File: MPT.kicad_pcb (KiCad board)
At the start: 2 copper layers, 60 x 50 mm, 94 parts, among them J1 USB4105GFA120, J2 ER-TFT2.79-1, Q2 BSS138, SW1 OS102011MA1QN1, SW2 KMR421GULCLFS, SW3 KMR421GULCLFS, SW4 SW_1825910-6, SW5 SW_1825910-6, SW6 SW_1825910-6, SW7 SW_1825910-6, U2 BQ25185, U3 BQ27441-G1, U4 ESP32-S3-WROOM-1-N4R2, U5 RCLAMP0854P.TCT, U6 TPS63030, U7 MIC2841A

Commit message: PCB Layout Connecting
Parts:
- moved D2 19.9 mm to (168.4, 91.7), turned to 90 degrees
- moved R20 19.5 mm to (170.0, 91.7), turned to 90 degrees
- moved R42 9.96 mm to (164.7, 114.5), turned to 90 degrees
- moved R38 8.91 mm to (175.8, 111.5), turned to 0 degrees
- moved C18 7.23 mm to (175.8, 113.1), turned to 180 degrees
- moved R39 7.10 mm to (171.8, 112.5), turned to 0 degrees
- moved C22 6.97 mm to (166.4, 114.5), turned to -90 degrees
- moved R40 6.73 mm to (179.8, 113.1), turned to 0 degrees
- moved C19 6.08 mm to (171.8, 114.1), turned to 180 degrees
- moved C21 6.06 mm to (183.4, 115.9), turned to 0 degrees
- moved C20 4.62 mm to (179.8, 114.7), turned to 180 degrees
- moved R41 4.14 mm to (183.4, 117.5), turned to 180 degrees
- moved R19 1.70 mm to (144.3, 107.8), turned to 0 degrees
- moved R43 1.31 mm to (139.8, 108.5)
- moved C12 1.00 mm to (174.4, 102.6)
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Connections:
- U4 pad 17: /MCU/GPIO_JOYSTICK_UP -> /MCU/RTC_INT
- U4 pad 18: /MCU/GPIO_JOYSTICK_RIGHT -> /MCU/GPIO_BUTTON1
- U4 pad 19: /MCU/GPIO_JOYSTICK_CENTER -> /MCU/GPIO_BUTTON2
- U4 pad 20: /MCU/GPIO_JOYSTICK_LEFT -> /MCU/GPIO_BUTTON3
- U4 pad 21: /MCU/GPIO_JOYSTICK_DOWN -> /MCU/GPIO_BUTTON4
- U4 pad 22: /MCU/RTC_INT -> /MCU/GPIO_JOYSTICK_DOWN
- U4 pad 23: Net-(D2-K) -> /MCU/GPIO_JOYSTICK_RIGHT
- U4 pad 24: unconnected-(U4-IO47-Pad24) -> /MCU/GPIO_JOYSTICK_UP
- U4 pad 25: unconnected-(U4-IO48-Pad25) -> /MCU/GPIO_JOYSTICK_CENTER
- U4 pad 31: /MCU/GPIO_BUTTON2 -> /MCU/GPIO_JOYSTICK_LEFT
- U4 pad 32: /MCU/GPIO_BUTTON3 -> unconnected-(U4-IO39-Pad32)
- U4 pad 33: /MCU/GPIO_BUTTON4 -> unconnected-(U4-IO40-Pad33)
- U4 pad 38: /MCU/GPIO_BUTTON1 -> Net-(D2-K)
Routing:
- net +3V4: track 1.44 -> 149.6 mm, vias 0 -> 14
- net /BMS/STAT2: track 2.67 -> 63.8 mm, vias 0 -> 4
- net /BMS/STAT1: track 3.03 -> 60.1 mm, vias 0 -> 2
- net VBAT: track 17.4 -> 66.5 mm, vias 2 -> 6
- net /MCU/GPIO_JOYSTICK_LEFT: track 0.00 -> 31.1 mm, vias 0 -> 3
- net /MCU/GPIO_BUTTON1: track 0.00 -> 29.2 mm, vias 0 -> 2
- net /MCU/GPIO_BUTTON2: track 0.00 -> 28.4 mm, vias 0 -> 2
- net /MCU/SLEEP_CTRL_PIN: track 0.00 -> 28.1 mm, vias 0 -> 4
- net /MCU/GPIO_JOYSTICK_DOWN: track 0.00 -> 25.3 mm, vias 0 -> 1
- net /MCU/GPIO_JOYSTICK_CENTER: track 0.00 -> 25.0 mm, vias 0 -> 3
- net /MCU/GPIO_JOYSTICK_RIGHT: track 0.00 -> 24.8 mm, vias 0 -> 3
- net /MCU/GPIO_JOYSTICK_UP: track 0.00 -> 22.2 mm, vias 0 -> 3
- net /MCU/GPIO_BUTTON4: track 0.00 -> 19.0 mm
- net /MCU/GPIO_BUTTON3: track 0.00 -> 18.8 mm, vias 0 -> 2
- net /MCU/RTC_INT: track 0.00 -> 17.2 mm, vias 0 -> 2
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
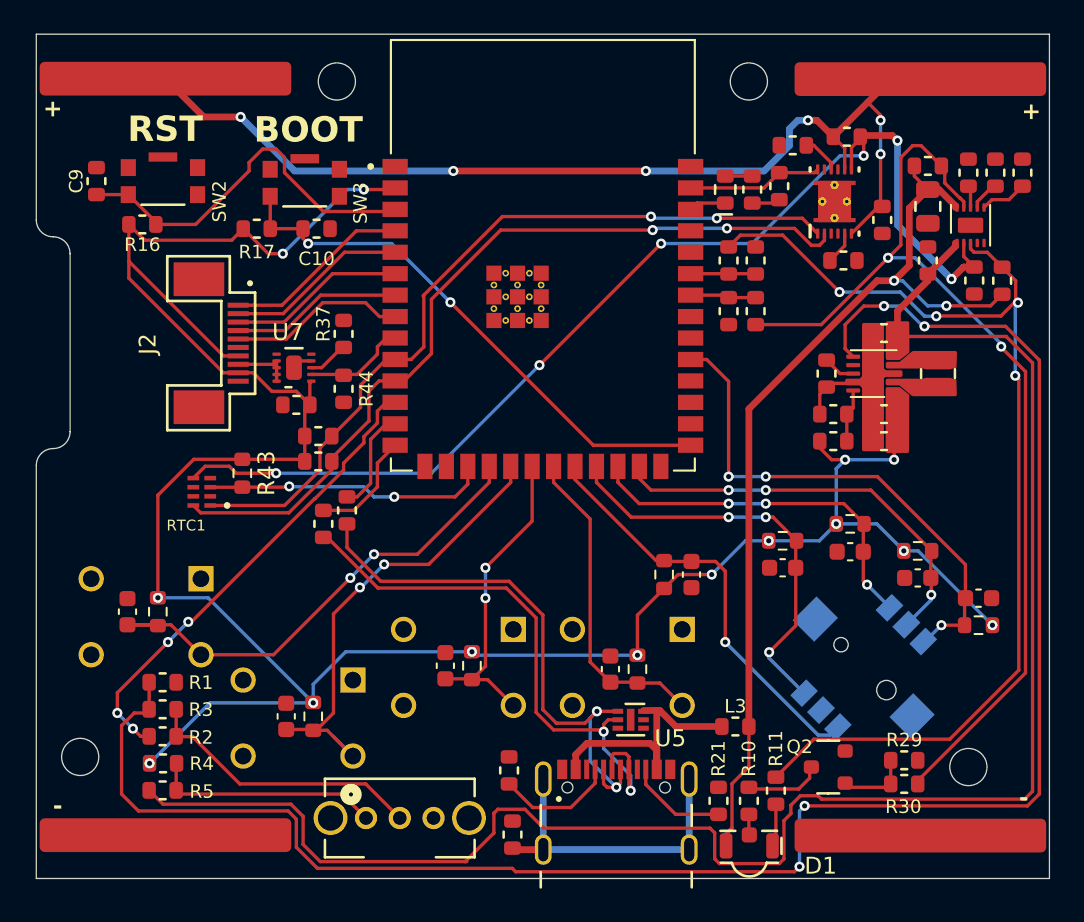
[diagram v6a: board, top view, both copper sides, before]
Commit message: Remove Via in Pad Lessen use of backside for routing of 3v4
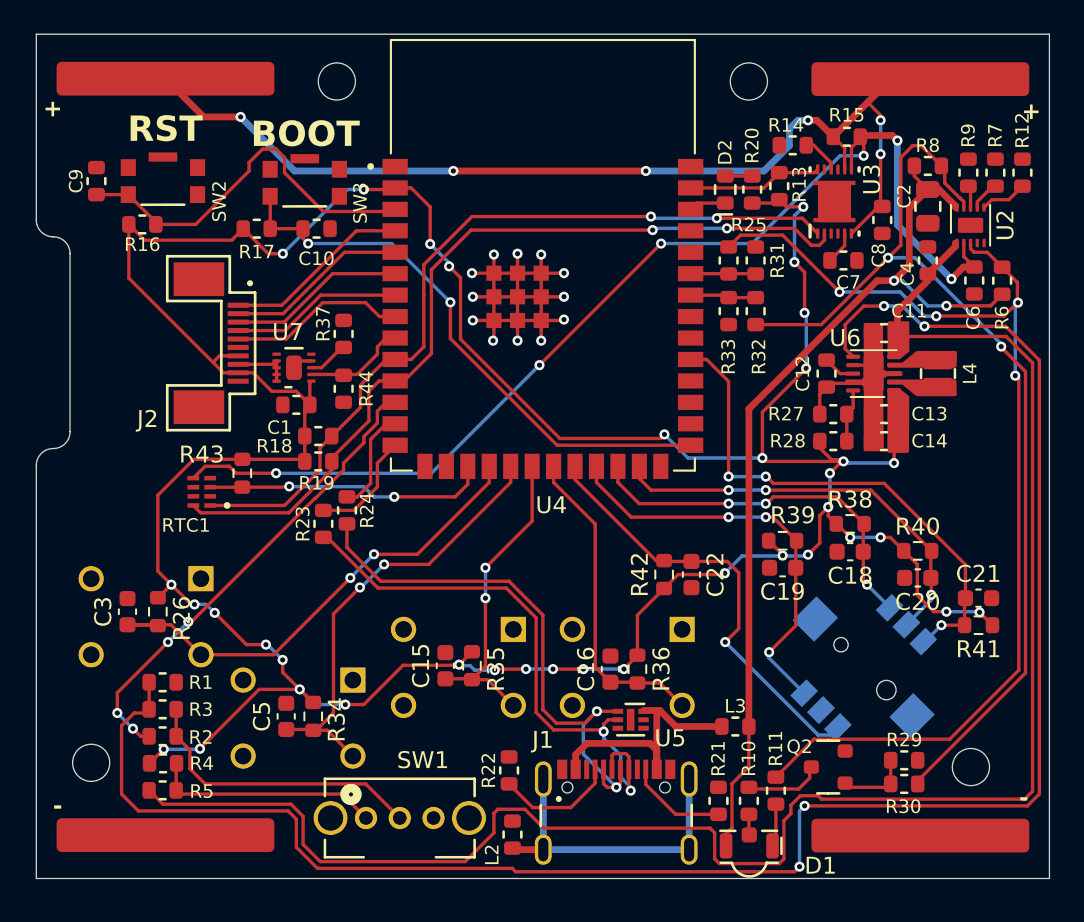
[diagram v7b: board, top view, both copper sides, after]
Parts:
- moved H2 0.74 mm to (130.8, 125.6)
- moved H3 0.15 mm to (182.9, 125.9)
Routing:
- net +3V4: track 149.6 -> 203.8 mm, vias 14 -> 36
- net GND: track 5.95 -> 39.0 mm, vias 0 -> 12
- net /MCU/GPIO_BUTTON2: track 28.4 -> 26.8 mm
- net /MCU/Boot Mode: track 32.5 -> 33.7 mm
- net /MCU/GPIO_JOYSTICK_DOWN: track 25.3 -> 26.3 mm
- net /BMS/I2C_SCL: track 48.8 -> 49.8 mm
- net /BMS/I2C_SDA: track 46.9 -> 47.9 mm
- net Net-(SW1-B): track 16.8 -> 17.5 mm

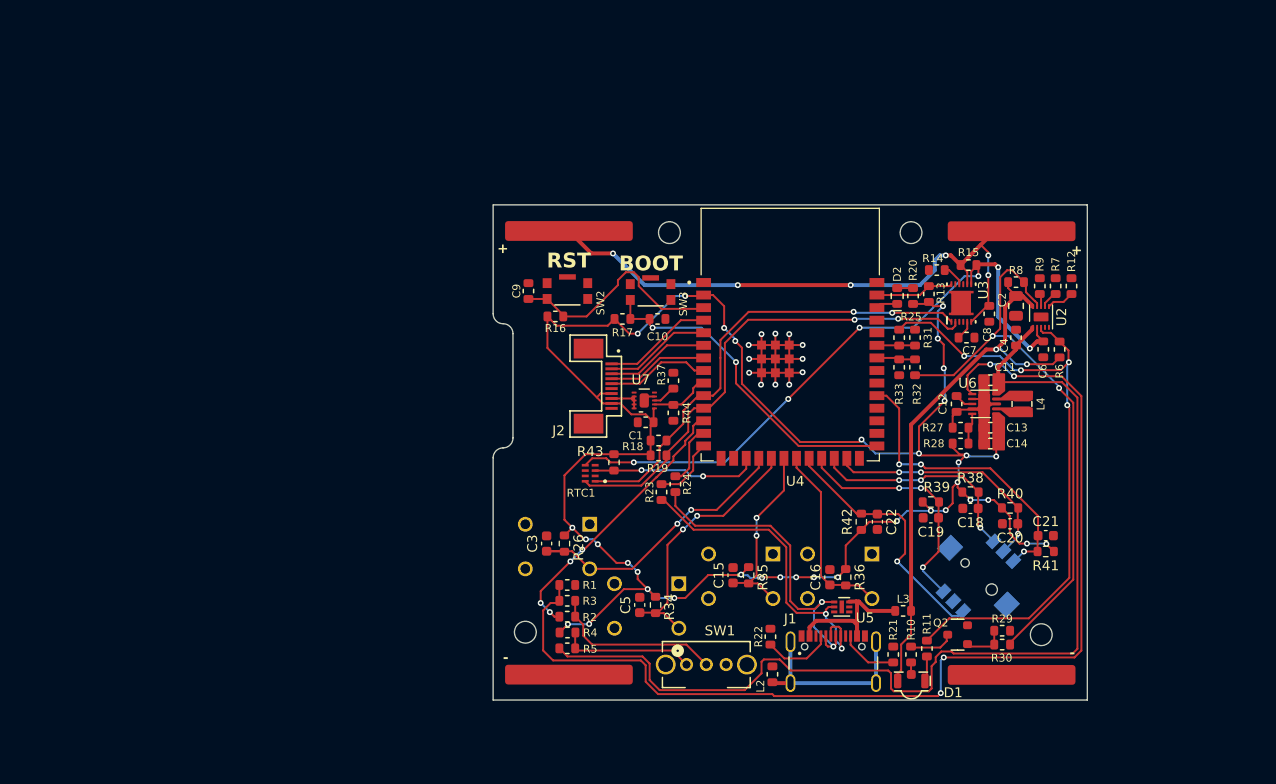
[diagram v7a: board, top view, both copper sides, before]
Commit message: Added GND Network and connected all components
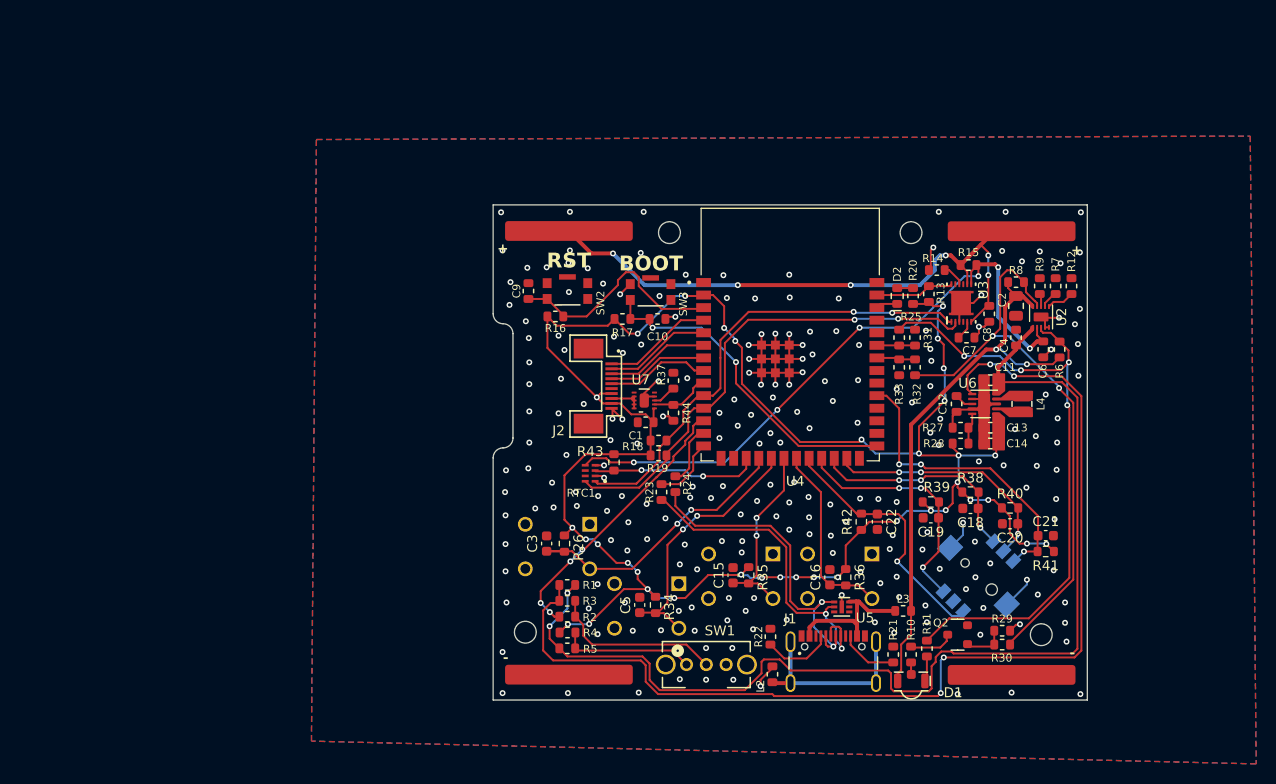
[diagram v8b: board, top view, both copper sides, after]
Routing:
- net GND: track 39.0 -> 75.3 mm, vias 12 -> 221
- net VSYS: track 103.6 -> 111.5 mm, vias 0 -> 2
- net +3V4: track 203.8 -> 202.5 mm
- added copper zone on B.Cu, net GND
- added copper zone on F.Cu, net GND
